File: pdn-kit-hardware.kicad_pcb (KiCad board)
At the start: 2 copper layers, 12 parts, among them U1 BQ25895RTWR, U2 TPS22917DBVR, U3 TPS63802DLAR, U4 MAX17055ETB+T

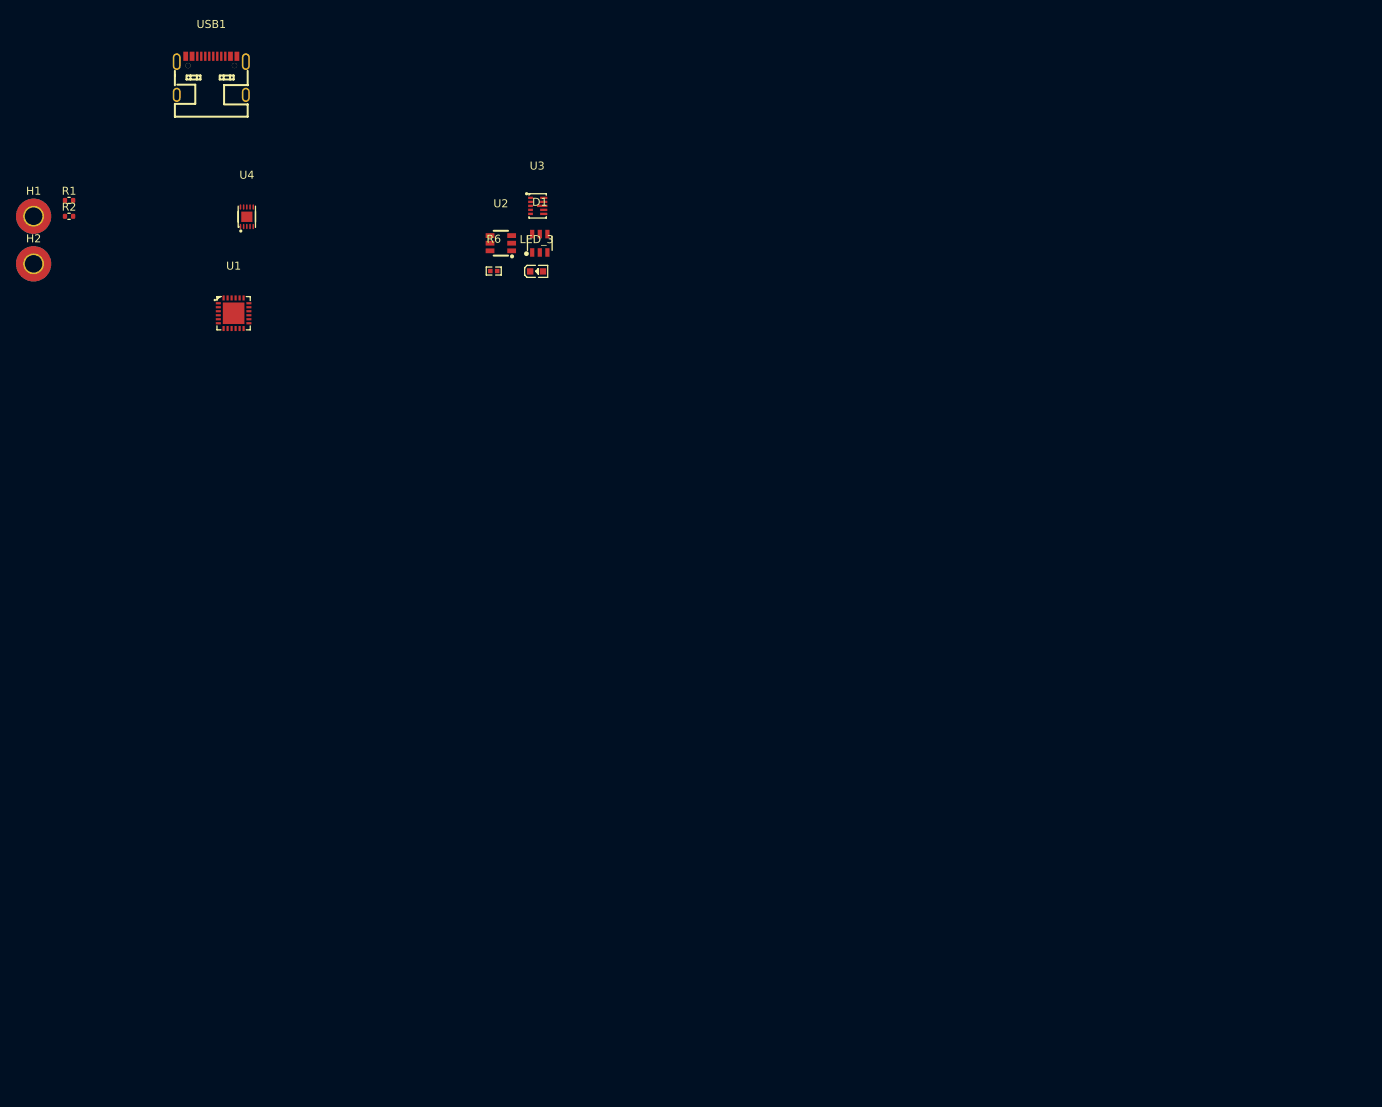
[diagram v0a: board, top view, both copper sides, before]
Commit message: Fix LED's -> anode wired to VCC, not GND.
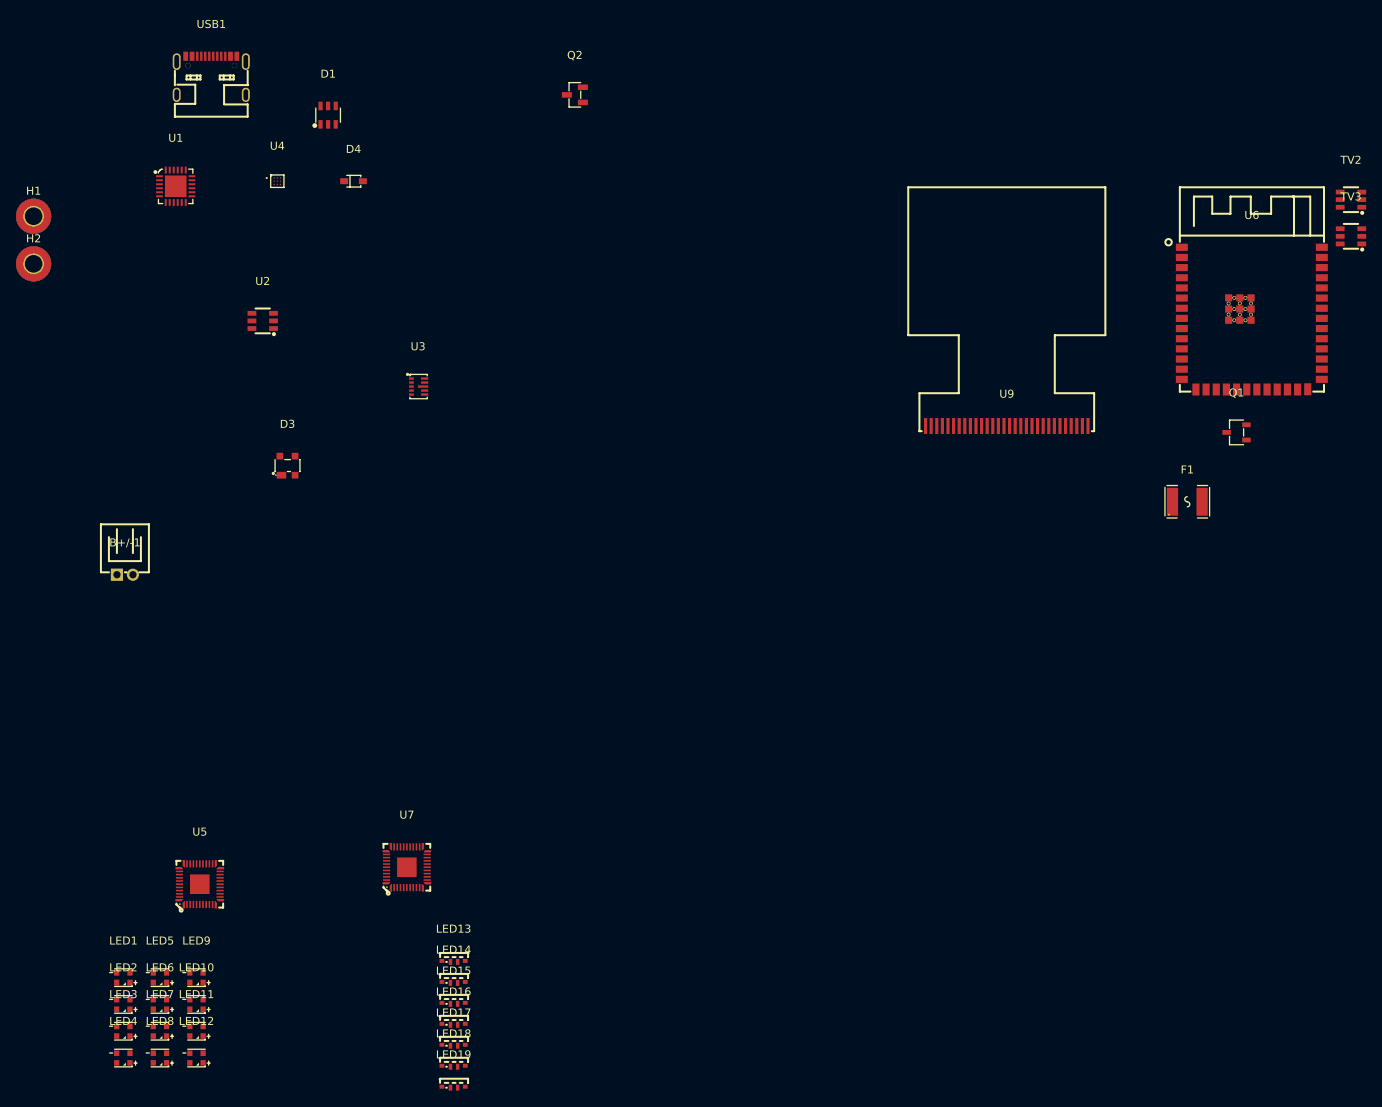
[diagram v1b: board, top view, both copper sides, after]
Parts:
- removed LED_3: GREEN, global:LED0603-RD_RED
- removed R1, R2: 5.1k, Resistor_SMD:R_0402_1005Metric
- removed R6: 1.2k, global:R0402
- added B+/-1: GH-2AW R, global:CONN-TH_2P-P2.00_PH-2AW, F.Cu at (80.0, 115.9)
- added D3: PRTR5V0U2X, global:SOT-143-4_L2.9-W1.3-P1.92-LS2.4-BL, F.Cu at (100.3, 102.2)
- added D4: LBAT54HT1G, global:SOD-323_L1.8-W1.3-LS2.5-RD, F.Cu at (108.6, 66.7)
- added F1: JK-MSMD500L-6, global:F1812, F.Cu at (212.8, 106.7)
- added LED1: NH-Z1921RGBA-SG, global:LED-ARRAY-SMD_4P-L2.2-W2.1-BR-RD, F.Cu at (79.8, 166.2)
- added LED10: NH-Z1921RGBA-SG, global:LED-ARRAY-SMD_4P-L2.2-W2.1-BR-RD, F.Cu at (89.0, 169.6)
- added LED11: NH-Z1921RGBA-SG, global:LED-ARRAY-SMD_4P-L2.2-W2.1-BR-RD, F.Cu at (89.0, 172.9)
- added LED12: NH-Z1921RGBA-SG, global:LED-ARRAY-SMD_4P-L2.2-W2.1-BR-RD, F.Cu at (89.0, 176.3)
- added LED13: LED_ARGB, global:LED-SMD_FM-3510RGBA-SG, F.Cu at (121.1, 164.2)
- added LED14: LED_ARGB, global:LED-SMD_FM-3510RGBA-SG, F.Cu at (121.1, 166.8)
- added LED15: LED_ARGB, global:LED-SMD_FM-3510RGBA-SG, F.Cu at (121.1, 169.4)
- added LED16: LED_ARGB, global:LED-SMD_FM-3510RGBA-SG, F.Cu at (121.1, 172.1)
- added LED17: LED_ARGB, global:LED-SMD_FM-3510RGBA-SG, F.Cu at (121.1, 174.7)
- added LED18: LED_ARGB, global:LED-SMD_FM-3510RGBA-SG, F.Cu at (121.1, 177.3)
- added LED19: LED_ARGB, global:LED-SMD_FM-3510RGBA-SG, F.Cu at (121.1, 179.9)
- added LED2: NH-Z1921RGBA-SG, global:LED-ARRAY-SMD_4P-L2.2-W2.1-BR-RD, F.Cu at (79.8, 169.6)
- added LED3: NH-Z1921RGBA-SG, global:LED-ARRAY-SMD_4P-L2.2-W2.1-BR-RD, F.Cu at (79.8, 172.9)
- added LED4: NH-Z1921RGBA-SG, global:LED-ARRAY-SMD_4P-L2.2-W2.1-BR-RD, F.Cu at (79.8, 176.3)
- added LED5: NH-Z1921RGBA-SG, global:LED-ARRAY-SMD_4P-L2.2-W2.1-BR-RD, F.Cu at (84.4, 166.2)
- added LED6: NH-Z1921RGBA-SG, global:LED-ARRAY-SMD_4P-L2.2-W2.1-BR-RD, F.Cu at (84.4, 169.6)
- added LED7: NH-Z1921RGBA-SG, global:LED-ARRAY-SMD_4P-L2.2-W2.1-BR-RD, F.Cu at (84.4, 172.9)
- added LED8: NH-Z1921RGBA-SG, global:LED-ARRAY-SMD_4P-L2.2-W2.1-BR-RD, F.Cu at (84.4, 176.3)
- added LED9: NH-Z1921RGBA-SG, global:LED-ARRAY-SMD_4P-L2.2-W2.1-BR-RD, F.Cu at (89.0, 166.2)
- added Q1: AO3415A, global:SOT-23-3_L2.9-W1.6-P1.90-LS2.8-BR, F.Cu at (219.0, 98.1)
- added Q2: BJT 2222A, global:SOT-23-3_L2.9-W1.3-P1.90-LS2.4-BR, F.Cu at (136.3, 55.9)
- added TV2: SRV05-4-P-T7, global:SOT-23-6_L2.9-W1.6-P0.95-LS2.8-BR, F.Cu at (233.3, 69.0)
- added TV3: SRV05-4-P-T7, global:SOT-23-6_L2.9-W1.6-P0.95-LS2.8-BR, F.Cu at (233.3, 73.6)
- added U5: IS31FL3236A-QFLS2-TR, global:QFN-44_L5.0-W5.0-P0.40-BL-EP, F.Cu at (89.4, 154.6)
- added U6: ESP32-S3-WROOM-1(N8R8), global:WIRELM-SMD_ESP32-S3-WROOM-1, F.Cu at (220.9, 83.8)
- added U7: IS31FL3236A-QFLS2-TR, global:QFN-44_L5.0-W5.0-P0.40-BL-EP, F.Cu at (115.3, 152.4)
- added U9: X096-2864KSWPG01-H30, global:OLED-SMD_X096-2864KSWPG01-H30, F.Cu at (190.2, 97.3)
- D1: value USBLC6-2SC6_C2827654 -> USBLC6-2SC6
- U1: value BQ25895RTWR -> BQ25619RTWR; footprint global:QFN-24_L4.0-W4.0-P0.50-TL-EP2.7 -> global:WQFN-24_L4.0-W4.0-P0.50-TL-EP2.7
- U4: value MAX17055ETB+T -> MAX17260SEWL; footprint global:TDFN-10_L2.5-W2.0-P0.40-BL-EP -> global:BGA-9_L1.5-W1.4-R3-C3-P0.40-TL
- moved U2 31.3 mm to (97.2, 84.1)
- moved D1 30.9 mm to (105.4, 58.4)
- moved U3 27.0 mm to (116.7, 92.3)
- moved U1 17.4 mm to (86.4, 67.3)
- moved U4 5.85 mm to (99.1, 66.7)
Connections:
- D1 pad 1: /Data_+ -> /power/D+
- D1 pad 2: /GND -> GND
- D1 pad 3: /Data_- -> /power/D-
- D1 pad 4: /Data_- -> /power/USB D-
- D1 pad 5: Net-(D1-VBUS) -> VBUS
- D1 pad 6: /Data_+ -> /power/USB D+
- U1 pad 1: unconnected-(U1-VBUS-Pad1) -> VBUS
- U1 pad 10: unconnected-(U1-ILIM-Pad10) -> +BATT
- U1 pad 11: unconnected-(U1-TS-Pad11) -> Net-(U1-TS)
- U1 pad 12: unconnected-(U1-QON-Pad12) -> Net-(U1-~{QON})
- U1 pad 13: unconnected-(U1-BAT-Pad13) -> /power/BATT_BQ
- U1 pad 14: unconnected-(U1-BAT-Pad14) -> /power/BATT_BQ
- U1 pad 15: unconnected-(U1-SYS-Pad15) -> VSYS
- U1 pad 16: unconnected-(U1-SYS-Pad16) -> VSYS
- U1 pad 17: unconnected-(U1-PGND-Pad17) -> GND
- U1 pad 18: unconnected-(U1-PGND-Pad18) -> GND
- U1 pad 19: unconnected-(U1-SW-Pad19) -> Net-(C7-Pad1)
- U1 pad 2: unconnected-(U1-D+-Pad2) -> GND
- U1 pad 20: unconnected-(U1-SW-Pad20) -> Net-(C7-Pad1)
- U1 pad 21: unconnected-(U1-BTST-Pad21) -> Net-(U1-BTST)
- U1 pad 22: unconnected-(U1-REGN-Pad22) -> /power/REGN
- U1 pad 23: unconnected-(U1-PMID-Pad23) -> Net-(U1-PMID)
- U1 pad 24: unconnected-(U1-DSEL-Pad24) -> VBUS
- U1 pad 25: unconnected-(U1-PAD-Pad25) -> GND
- U1 pad 3: unconnected-(U1-D–-Pad3) -> Net-(U1-PMID_GOOD)
- U1 pad 4: unconnected-(U1-STAT-Pad4) -> Net-(U1-STAT)
- U1 pad 5: unconnected-(U1-SCL-Pad5) -> /LEDs/I2C_SCL
- U1 pad 6: unconnected-(U1-SDA-Pad6) -> /LEDs/I2C_SDA
- U1 pad 7: unconnected-(U1-INT-Pad7) -> /power/INT
- U1 pad 9: unconnected-(U1-CE-Pad9) -> /power/CE
- U2 pad 1: unconnected-(U2-VIN-Pad1) -> VSYS
- U2 pad 2: unconnected-(U2-GND-Pad2) -> GND
- U2 pad 3: unconnected-(U2-ON-Pad3) -> Net-(D2-K)
- U2 pad 4: unconnected-(U2-CT-Pad4) -> Net-(U2-CT)
- U2 pad 5: unconnected-(U2-QOD-Pad5) -> VCC
- U2 pad 6: unconnected-(U2-VOUT-Pad6) -> VCC
- U3 pad 1: unconnected-(U3-EN-Pad1) -> VCC
- U3 pad 10: unconnected-(U3-VIN-Pad10) -> VCC
- U3 pad 2: unconnected-(U3-MODE-Pad2) -> GND
- U3 pad 3: unconnected-(U3-AGND-Pad3) -> GND
- U3 pad 4: unconnected-(U3-FB-Pad4) -> Net-(U3-FB)
- U3 pad 5: unconnected-(U3-PG-Pad5) -> Net-(U3-PG)
- U3 pad 6: unconnected-(U3-VOUT-Pad6) -> +3V3
- U3 pad 7: unconnected-(U3-L2-Pad7) -> Net-(U3-L2)
- U3 pad 8: unconnected-(U3-GND-Pad8) -> GND
- U3 pad 9: unconnected-(U3-L1-Pad9) -> Net-(U3-L1)
- USB1 pad A1B12: /GND -> GND
- USB1 pad A4B9: Net-(D1-VBUS) -> VBUS
- USB1 pad A6: /Data_+ -> /power/USB D+
- USB1 pad A7: /Data_- -> /power/USB D-
- USB1 pad B1A12: /GND -> GND
- USB1 pad B4A9: Net-(D1-VBUS) -> VBUS
- USB1 pad B6: /Data_+ -> /power/USB D+
- USB1 pad B7: /Data_- -> /power/USB D-
